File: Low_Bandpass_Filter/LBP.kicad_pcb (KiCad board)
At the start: 2 copper layers, 14 parts

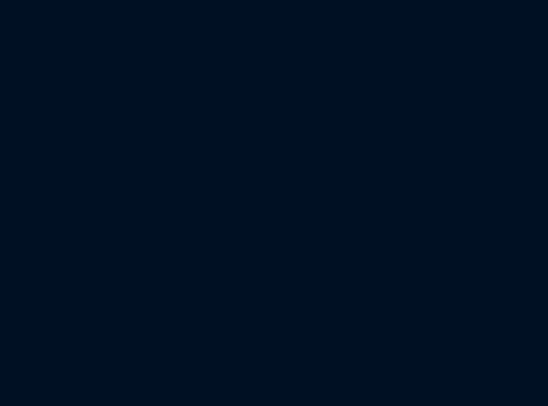
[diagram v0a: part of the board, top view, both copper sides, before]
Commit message: few mods
changed 4 single op amps to 1 big 4 op amp
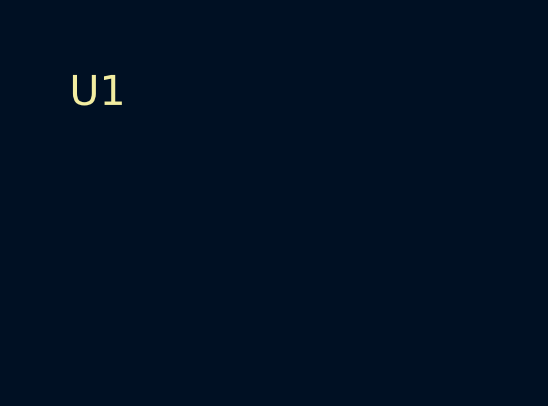
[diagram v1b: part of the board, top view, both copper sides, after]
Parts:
- added U1: OPA1641, OPA1644:SOP65P640X120-14N, F.Cu at (-44.7, -94.0)
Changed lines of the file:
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@@
 		)
+	)
+	(footprint "OPA1644:SOP65P640X120-14N"
+		(layer "F.Cu")
+		(at -44.696505 -94.017922)
+		(property "Reference" "U1"
+			(at 0 -0.5 0)
+			(unlocked yes)
+			(layer "F.SilkS")
+			(effects
+				(font
+					(size 1 1)
+					(thickness 0.1)
+				)
+			)
+		)
+		(property "Value" "OPA1641"
+			(at 0 1 0)
+			(unlocked yes)
+			(layer "F.Fab")
+			(effects
+				(font
+					(size 1 1)
+					(thickness 0.15)
+				)
+			)
+		)
+		(property "Datasheet" "http://www.ti.com/lit/ds/symlink/opa1641.pdf"
+			(at 0 0 0)
+			(unlocked yes)
+			(layer "F.Fab")
+			(hide yes)
+			(effects
+				(font
+					(size 1 1)
+					(thickness 0.15)
+				)
+			)
+		)
+		(property "Description" "JFET input, ultralow distortion, low-noise operational amplifier, SOIC-8/VSSOP-8"
+			(at 0 0 0)
+			(unlocked yes)
+			(layer "F.Fab")
+			(hide yes)
+			(effects
+				(font
+					(size 1 1)
+					(thickness 0.15)
+				)
+			)
+		)
+		(property ki_fp_filters "SOIC*3.9x4.9mm*P1.27mm* VSSOP*3x3mm*P0.65mm*")
+		(sheetname "/")
+		(sheetfile "LBP.kicad_sch")
+		(attr smd)
+		(fp_text user "${REFERENCE}"
+			(at 0 2.5 0)
+			(unlocked yes)
+			(layer "F.Fab")
+			(effects
+				(font
+					(size 1 1)
+					(thickness 0.15)
+				)
+			)
+		)
+		(embedded_fonts no)
 	)
 	(footprint "Resistor_THT:R_Axial_DIN0207_L6.3mm_D2.5mm_P10.16mm_Horizontal"
